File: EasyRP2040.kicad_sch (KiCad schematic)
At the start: 33 parts, among them J1 USB_C_Receptacle_USB2.0_14P, J2 Conn_01x20, J3 Conn_01x20, J4 Conn_01x03, SW1 SW_Push, U1 RP2040, U2 MCP1700x-330xxTT, U3 W25Q128JVS, Y1 12MHz

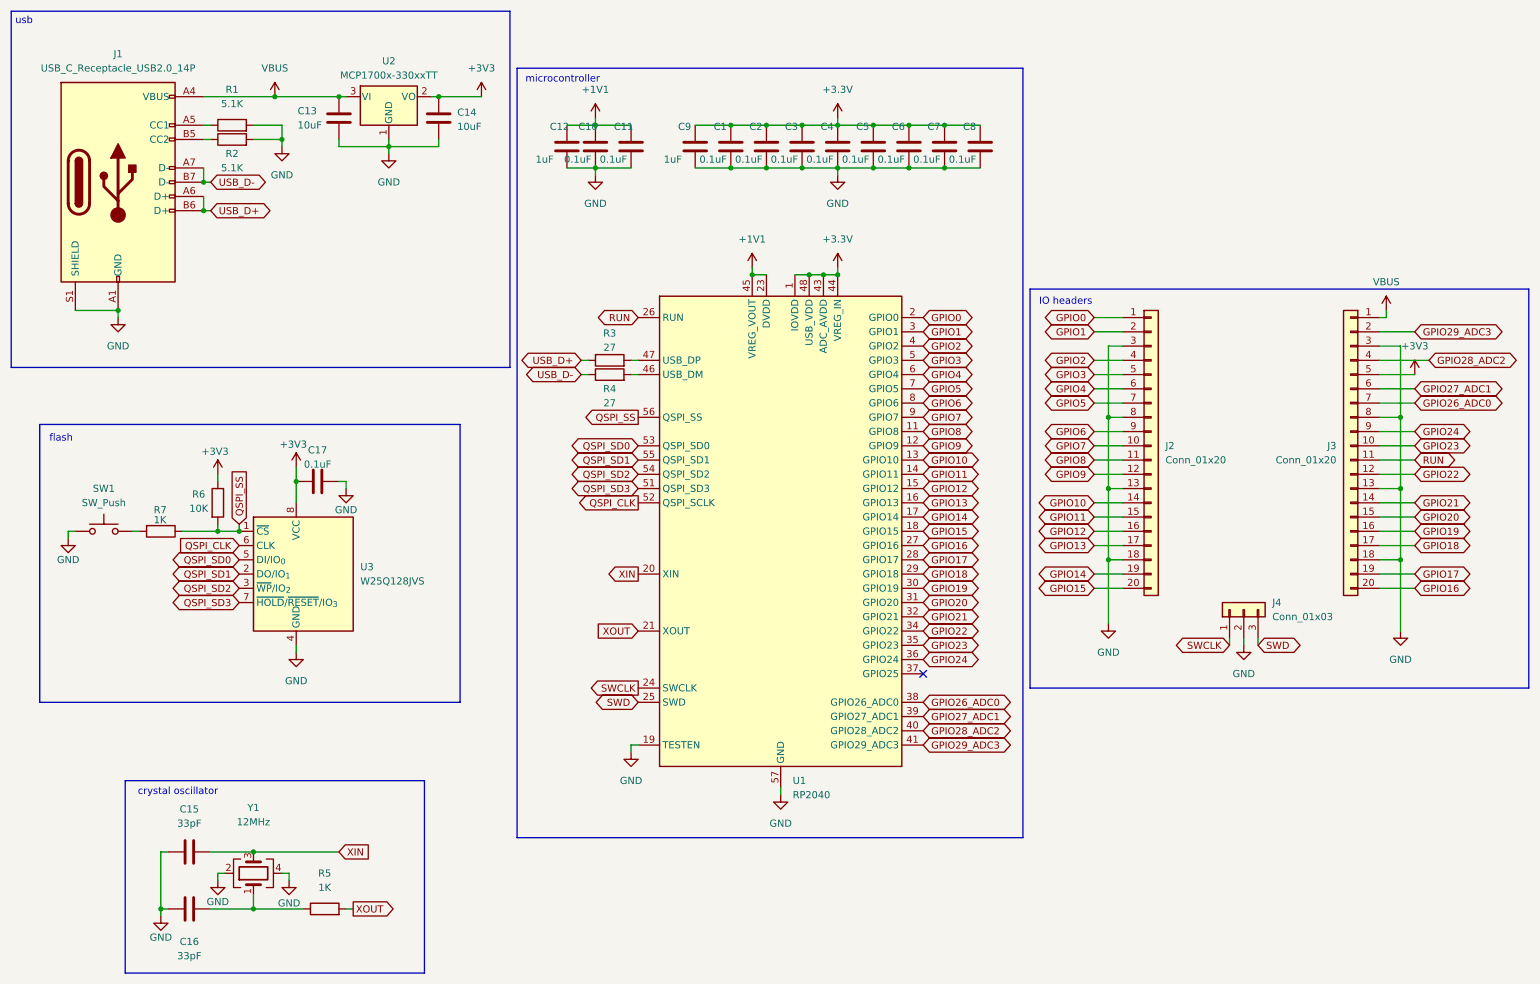
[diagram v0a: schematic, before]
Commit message: added imu + leds to schematic
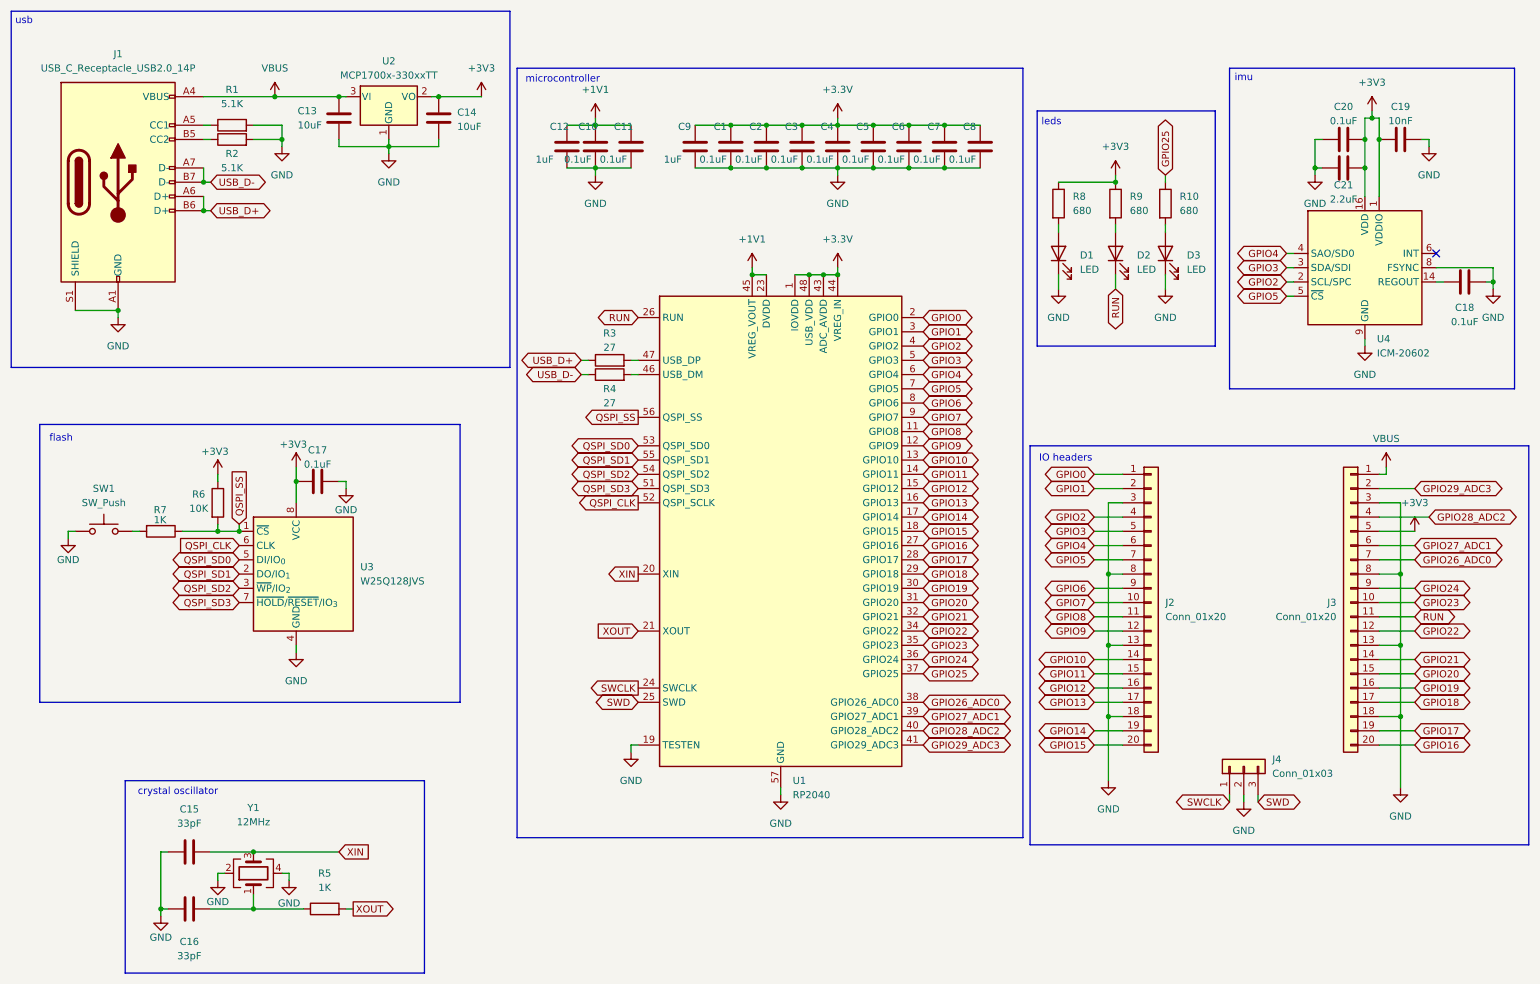
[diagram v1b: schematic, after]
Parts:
- added C18, C20: 0.1uF, symbol Device:C
- added C19: 10nF, symbol Device:C
- added C21: 2.2uF, symbol Device:C
- added D1, D2, D3: LED, symbol Device:LED
- added R10, R8, R9: 680, symbol Device:R
- added U4: ICM-20602, Package_LGA:LGA-16_3x3mm_P0.5mm_LayoutBorder3x5y, symbol Sensor_Motion:ICM-20602
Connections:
- net +3V3: now also C19.1, C20.2, C21.2, R8.1, R9.1, U4.1 (VDDIO), U4.16 (VDD)
- net GND: now also C18.2, C19.2, C20.1, C21.1, D1.1 (K), D3.1 (K), U4.10 (GND), U4.11 (GND), U4.12 (GND), U4.13 (GND), U4.15 (GND), U4.8 (FSYNC), U4.9 (GND)
- net GPIO2: now also U4.2 (SCL/SPC)
- net GPIO3: now also U4.3 (SDA/SDI)
- net GPIO4: now also U4.4 (SAO/SD0)
- net GPIO5: now also U4.5 (~{CS})
- net RUN: now also D2.1 (K)
- net GPIO25: now reaches U1.37 (GPIO25)
- net GPIO25: now also R10.1
- new net: D1.2 (A), R8.2
- new net: D2.2 (A), R9.2
- new net: D3.2 (A), R10.2
- new net: C18.1, U4.14 (REGOUT)
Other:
- note added: "imu"
- note added: "leds"
- moved on the sheet: J2, J3, J4

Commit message: done
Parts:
- C1, C10, C11, C12, C15, C16, C17, C18, C19, C2, C20, C21, C3, C4, C5, C6, C7, C8, C9: footprint (none) -> Capacitor_SMD:C_0402_1005Metric
- C13, C14: footprint (none) -> Capacitor_SMD:C_0201_0603Metric
- D1, D2, D3: footprint (none) -> LED_SMD:LED_0603_1608Metric
- J1: footprint (none) -> Connector_USB:USB_C_Receptacle_HRO_TYPE-C-31-M-12
- J2, J3: footprint (none) -> Connector_PinHeader_2.54mm:PinHeader_1x20_P2.54mm_Vertical
- J4: footprint (none) -> Connector_PinHeader_2.54mm:PinHeader_1x03_P2.54mm_Vertical
- R1, R10, R2, R3, R4, R5, R6, R7, R8, R9: footprint (none) -> Resistor_SMD:R_0402_1005Metric
- SW1: footprint (none) -> Button_Switch_SMD:SW_Push_SPST_NO_Alps_SKRK
- U3: footprint Package_SO:SOIC-8_5.3x5.3mm_P1.27mm -> Package_SON:Winbond_USON-8-1EP_3x2mm_P0.5mm_EP0.2x1.6mm
- Y1: footprint (none) -> Crystal:Crystal_SMD_3225-4Pin_3.2x2.5mm
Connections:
- net +3.3V is gone; now on net +3V3: C1.1, C2.1, C3.1, C4.1, C5.1, C6.1, C7.1, C8.1, C9.1, U1.1 (IOVDD), U1.10 (IOVDD), U1.22 (IOVDD), U1.33 (IOVDD), U1.42 (IOVDD), U1.43 (ADC_AVDD), U1.44 (VREG_IN), U1.48 (USB_VDD), U1.49 (IOVDD)

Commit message: fixed c13 c14
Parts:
- C13, C14: footprint Capacitor_SMD:C_0201_0603Metric -> Capacitor_SMD:C_0603_1608Metric
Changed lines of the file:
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@@
 			)
 		)
-		(property "Footprint" "Capacitor_SMD:C_0201_0603Metric"
+		(property "Footprint" "Capacitor_SMD:C_0603_1608Metric"
 			(at 72.0852 35.56 0)
 			(effects
@@
 			)
 		)
-		(property "Footprint" "Capacitor_SMD:C_0201_0603Metric"
+		(property "Footprint" "Capacitor_SMD:C_0603_1608Metric"
 			(at 89.8652 35.56 0)
 			(effects
